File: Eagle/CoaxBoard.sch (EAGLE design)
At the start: 7 parts, among them U1 SN74HC04_INVERTER

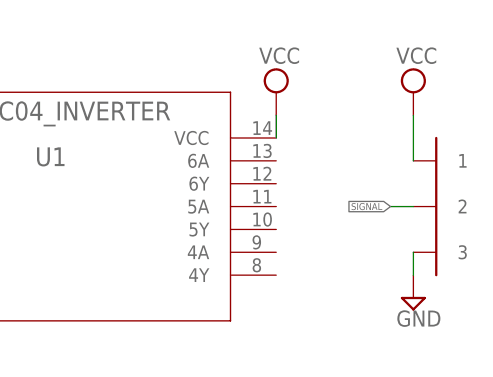
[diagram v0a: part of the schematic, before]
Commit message: design ordered from Oshpark
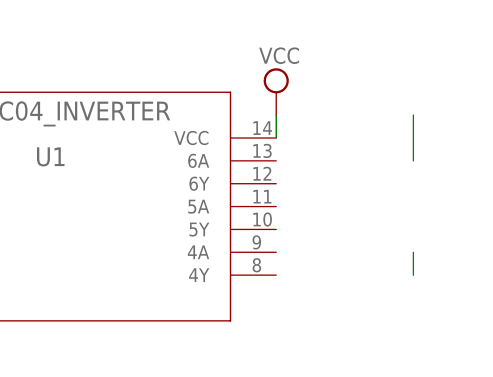
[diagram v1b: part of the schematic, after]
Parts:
- removed U$2: 1X3HEADER, 1x2HEADER:1X3HEADER
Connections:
- net GND: no longer U$2.3
- net SIGNAL: no longer U$2.2
- net VCC: no longer U$2.1
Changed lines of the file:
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@@
 <part name="C1" library="rcl" library_urn="urn:adsk.eagle:library:334" deviceset="C-EU" device="C0805" package3d_urn="urn:adsk.eagle:package:23617/2" value="10n"/>
 <part name="SUPPLY3" library="supply2" library_urn="urn:adsk.eagle:library:372" deviceset="VCC" device=""/>
-<part name="SUPPLY4" library="supply2" library_urn="urn:adsk.eagle:library:372" deviceset="VCC" device=""/>
 <part name="SUPPLY5" library="supply2" library_urn="urn:adsk.eagle:library:372" deviceset="GND" device=""/>
-<part name="U$2" library="1x2HEADER" deviceset="1X3HEADER" device=""/>
-<part name="SUPPLY6" library="supply2" library_urn="urn:adsk.eagle:library:372" deviceset="GND" device=""/>
 </parts>
 <sheets>
@@
 <attribute name="VALUE" x="125.095" y="26.035" size="1.778" layer="96"/>
 </instance>
-<instance part="SUPPLY4" gate="G$1" x="142.24" y="22.86" smashed="yes">
-<attribute name="VALUE" x="140.335" y="26.035" size="1.778" layer="96"/>
-</instance>
 <instance part="SUPPLY5" gate="GND" x="38.1" y="10.16" smashed="yes">
 <attribute name="VALUE" x="36.195" y="6.985" size="1.778" layer="96"/>
-</instance>
-<instance part="U$2" gate="G$1" x="147.32" y="10.16" smashed="yes"/>
-<instance part="SUPPLY6" gate="GND" x="142.24" y="0" smashed="yes">
-<attribute name="VALUE" x="140.335" y="-3.175" size="1.778" layer="96"/>
 </instance>
 </instances>
@@
 <pinref part="SUPPLY1" gate="GND" pin="GND"/>
 <wire x1="76.2" y1="0" x2="76.2" y2="2.54" width="0.1524" layer="91"/>
-</segment>
-<segment>
-<pinref part="U$2" gate="G$1" pin="3"/>
-<pinref part="SUPPLY6" gate="GND" pin="GND"/>
-<wire x1="142.24" y1="2.54" x2="142.24" y2="5.08" width="0.1524" layer="91"/>
 </segment>
 </net>
@@
 <wire x1="127" y1="20.32" x2="127" y2="17.78" width="0.1524" layer="91"/>
 </segment>
-<segment>
-<pinref part="U$2" gate="G$1" pin="1"/>
-<pinref part="SUPPLY4" gate="G$1" pin="VCC"/>
-<wire x1="142.24" y1="20.32" x2="142.24" y2="15.24" width="0.1524" layer="91"/>
-</segment>
 </net>
 <net name="N$6" class="0">
@@
 <net name="SIGNAL" class="0">
 <segment>
-<pinref part="U$2" gate="G$1" pin="2"/>
-<wire x1="142.24" y1="10.16" x2="139.7" y2="10.16" width="0.1524" layer="91"/>
-<label x="139.7" y="10.16" size="0.762" layer="95" rot="R180" xref="yes"/>
-</segment>
-<segment>
 <pinref part="U1" gate="A" pin="2Y"/>
 <wire x1="76.2" y1="10.16" x2="78.74" y2="10.16" width="0.1524" layer="91"/>
@@
 </segment>
 </net>
+<net name="N$4" class="0">
+<segment>
+<wire x1="142.24" y1="20.32" x2="142.24" y2="15.24" width="0.1524" layer="91"/>
+</segment>
+</net>
+<net name="N$5" class="0">
+<segment>
+<wire x1="142.24" y1="2.54" x2="142.24" y2="5.08" width="0.1524" layer="91"/>
+</segment>
+</net>

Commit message: updates to eagle files
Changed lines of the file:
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@@
-</segment>
-</net>
-<net name="N$4" class="0">
-<segment>
-<wire x1="142.24" y1="20.32" x2="142.24" y2="15.24" width="0.1524" layer="91"/>
-</segment>
-</net>
-<net name="N$5" class="0">
-<segment>
-<wire x1="142.24" y1="2.54" x2="142.24" y2="5.08" width="0.1524" layer="91"/>
 </segment>
 </net>
